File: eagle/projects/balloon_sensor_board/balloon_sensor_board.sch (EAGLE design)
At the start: 13 parts, among them J201 MOL-SL-4-RA, U1 PCT2075GVJ, U202 MS560702BA03-50

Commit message: cleaned up HAT and balloon_sensor for panelling
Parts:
- added TP202: (no value), daqcs:TEST_POINT_SMT_15R_SMD
- renumbered LOGO1 to LOGO201, LOGO2 to LOGO202, U1 to U201
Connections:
- net GND: now also TP201.TP
- net TEMP0_OS: now also TP202.TP; no longer TP201.TP
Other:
- note added: "1"
- note added: "DESIGN: 001-004-01"
- note removed: "A"
- moved on the sheet: TP201
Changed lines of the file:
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@@
 </variantdefs>
 <classes>
-<class number="0" name="default" width="0" drill="0">
+<class number="0" name="default" width="0" drill="0.381">
+<clearance class="0" value="0.1524"/>
 </class>
 </classes>
@@
 <part name="PP3V3201" library="daqcs" deviceset="PP3V3" device=""/>
 <part name="C201" library="daqcs" deviceset="CAP" device="_0603" technology="_1UF0" value="1uF"/>
-<part name="GND202" library="daqcs" deviceset="GND" device=""/>
+<part name="GND203" library="daqcs" deviceset="GND" device=""/>
 <part name="U202" library="daqcs" deviceset="MS5607" device="_8SMD" technology="-02BA03" value="MS560702BA03-50"/>
 <part name="R204" library="daqcs" deviceset="RES" device="_0603" technology="_0R0" value="0.0"/>
 <part name="C203" library="daqcs" deviceset="CAP" device="_0603" technology="_100NF0" value="100nF"/>
-<part name="GND204" library="daqcs" deviceset="GND" device=""/>
-<part name="GND206" library="daqcs" deviceset="GND" device=""/>
+<part name="GND205" library="daqcs" deviceset="GND" device=""/>
+<part name="GND207" library="daqcs" deviceset="GND" device=""/>
 <part name="GND209" library="daqcs" deviceset="GND" device=""/>
 <part name="C202" library="daqcs" deviceset="CAP" device="_0603" technology="_100NF0" value="100nF"/>
 <part name="R203" library="daqcs" deviceset="RES" device="_0603" technology="_0R0" value="0.0"/>
-<part name="GND205" library="daqcs" deviceset="GND" device=""/>
+<part name="GND206" library="daqcs" deviceset="GND" device=""/>
 <part name="GND208" library="daqcs" deviceset="GND" device=""/>
-<part name="GND203" library="daqcs" deviceset="GND" device=""/>
-<part name="TP201" library="daqcs" deviceset="TEST_POINT_SMT" device="_15R_SMD"/>
+<part name="GND204" library="daqcs" deviceset="GND" device=""/>
+<part name="TP202" library="daqcs" deviceset="TEST_POINT_SMT" device="_15R_SMD"/>
 <part name="PP3V3202" library="daqcs" deviceset="PP3V3" device=""/>
 <part name="PP3V3203" library="daqcs" deviceset="PP3V3" device=""/>
-<part name="U1" library="daqcs" deviceset="PCT2075GV" device="_TSOP6" value="PCT2075GVJ"/>
-<part name="LOGO1" library="daqcs" deviceset="SQUAD_LOGO" device=""/>
-<part name="LOGO2" library="daqcs" deviceset="CMS_LOGO" device=""/>
+<part name="U201" library="daqcs" deviceset="PCT2075GV" device="_TSOP6" value="PCT2075GVJ"/>
+<part name="LOGO201" library="daqcs" deviceset="SQUAD_LOGO" device=""/>
+<part name="LOGO202" library="daqcs" deviceset="CMS_LOGO" device=""/>
+<part name="TP201" library="daqcs" deviceset="TEST_POINT_SMT" device="_15R_SMD"/>
+<part name="GND202" library="daqcs" deviceset="GND" device=""/>
 </parts>
 <sheets>
@@
 <text x="81.28" y="182.88" size="3.81" layer="91">I2C_SENSORS</text>
 <text x="330.2" y="27.94" size="3.81" layer="91">TITLE_TOC</text>
-<text x="421.64" y="7.62" size="3.81" layer="91">A</text>
+<text x="421.64" y="7.62" size="3.81" layer="91">1</text>
 <text x="327.66" y="60.96" size="3.81" layer="91">ENGINEER: CHRIS SCHWAB</text>
 <text x="340.36" y="68.58" size="3.81" layer="91">TEAM: P17105</text>
+<text x="335.28" y="76.2" size="3.81" layer="91">DESIGN: 001-004-01</text>
 </plain>
 <instances>
@@
 <text x="86.36" y="251.46" size="11.43" layer="91">TEMP AND PRESSURE SENSORS</text>
 <text x="330.2" y="27.94" size="3.81" layer="91">I2C_SENSORS</text>
-<text x="421.64" y="7.62" size="3.81" layer="91">A</text>
+<text x="421.64" y="7.62" size="3.81" layer="91">1</text>
 <text x="243.84" y="109.22" size="3.81" layer="91">Pressure Sensor 0</text>
 <text x="231.14" y="50.8" size="1.778" layer="91">Complement of CSB</text>
@@
 <attribute name="VOLTAGE" x="75.819" y="161.544" size="1.778" layer="95" ratio="10" rot="R90"/>
 </instance>
-<instance part="GND202" gate="1" x="81.28" y="154.94"/>
+<instance part="GND203" gate="1" x="81.28" y="154.94"/>
 <instance part="U202" gate="G$1" x="251.46" y="78.74"/>
 <instance part="R204" gate="G$1" x="218.44" y="53.34" rot="R90"/>
@@
 <attribute name="VOLTAGE" x="225.679" y="87.884" size="1.778" layer="95" ratio="10" rot="R90"/>
 </instance>
-<instance part="GND204" gate="1" x="203.2" y="81.28"/>
-<instance part="GND206" gate="1" x="218.44" y="40.64"/>
+<instance part="GND205" gate="1" x="203.2" y="81.28"/>
+<instance part="GND207" gate="1" x="218.44" y="40.64"/>
 <instance part="GND209" gate="1" x="274.32" y="40.64"/>
 <instance part="C202" gate="G$1" x="215.9" y="190.5" smashed="yes" rot="R90">
@@
 </instance>
 <instance part="R203" gate="G$1" x="210.82" y="165.1" rot="R90"/>
-<instance part="GND205" gate="1" x="210.82" y="152.4"/>
+<instance part="GND206" gate="1" x="210.82" y="152.4"/>
 <instance part="GND208" gate="1" x="271.78" y="152.4"/>
-<instance part="GND203" gate="1" x="198.12" y="185.42"/>
-<instance part="TP201" gate="G$1" x="304.8" y="177.8" smashed="yes" rot="R270">
-<attribute name="NAME" x="309.88" y="179.07" size="1.778" layer="95" align="center"/>
+<instance part="GND204" gate="1" x="198.12" y="185.42"/>
+<instance part="TP202" gate="G$1" x="304.8" y="177.8" smashed="yes" rot="R270">
+<attribute name="NAME" x="312.42" y="179.07" size="1.778" layer="95" align="center"/>
 <attribute name="TP_SIGNAL_NAME" x="303.53" y="173.99" size="1.778" layer="97" rot="R270"/>
 </instance>
 <instance part="PP3V3202" gate="G$1" x="226.06" y="210.82"/>
 <instance part="PP3V3203" gate="G$1" x="228.6" y="106.68"/>
-<instance part="U1" gate="G$1" x="248.92" y="182.88"/>
-<instance part="LOGO1" gate="G$1" x="96.52" y="66.04"/>
-<instance part="LOGO2" gate="G$1" x="96.52" y="48.26"/>
+<instance part="U201" gate="G$1" x="248.92" y="182.88"/>
+<instance part="LOGO201" gate="G$1" x="96.52" y="66.04"/>
+<instance part="LOGO202" gate="G$1" x="96.52" y="48.26"/>
+<instance part="TP201" gate="G$1" x="81.28" y="119.38" smashed="yes" rot="R270">
+<attribute name="NAME" x="88.9" y="120.65" size="1.778" layer="95" align="center"/>
+<attribute name="TP_SIGNAL_NAME" x="80.01" y="115.57" size="1.778" layer="97" rot="R270"/>
+</instance>
+<instance part="GND202" gate="1" x="68.58" y="114.3"/>
 </instances>
 <busses>
@@
 <junction x="226.06" y="190.5"/>
 <pinref part="PP3V3202" gate="G$1" pin="PP3V3"/>
-<pinref part="U1" gate="G$1" pin="VCC"/>
+<pinref part="U201" gate="G$1" pin="VCC"/>
 </segment>
 <segment>
@@
 <segment>
 <pinref part="C201" gate="G$1" pin="2"/>
-<pinref part="GND202" gate="1" pin="GND"/>
+<pinref part="GND203" gate="1" pin="GND"/>
 <wire x1="71.12" y1="160.02" x2="81.28" y2="160.02" width="0.1524" layer="91"/>
 <wire x1="81.28" y1="160.02" x2="81.28" y2="157.48" width="0.1524" layer="91"/>
 </segment>
 <segment>
-<pinref part="GND204" gate="1" pin="GND"/>
+<pinref part="GND205" gate="1" pin="GND"/>
 <pinref part="C203" gate="G$1" pin="1"/>
 <wire x1="203.2" y1="83.82" x2="203.2" y2="86.36" width="0.1524" layer="91"/>
@@
 <segment>
 <pinref part="R204" gate="G$1" pin="1"/>
-<pinref part="GND206" gate="1" pin="GND"/>
+<pinref part="GND207" gate="1" pin="GND"/>
 <wire x1="218.44" y1="48.26" x2="218.44" y2="43.18" width="0.1524" layer="91"/>
 </segment>
@@
 <pinref part="C202" gate="G$1" pin="1"/>
 <wire x1="210.82" y1="190.5" x2="198.12" y2="190.5" width="0.1524" layer="91"/>
-<pinref part="GND203" gate="1" pin="GND"/>
+<pinref part="GND204" gate="1" pin="GND"/>
 <wire x1="198.12" y1="190.5" x2="198.12" y2="187.96" width="0.1524" layer="91"/>
 </segment>
 <segment>
-<pinref part="GND205" gate="1" pin="GND"/>
+<pinref part="GND206" gate="1" pin="GND"/>
 <pinref part="R203" gate="G$1" pin="1"/>
 <wire x1="210.82" y1="154.94" x2="210.82" y2="160.02" width="0.1524" layer="91"/>
@@
 <pinref part="GND208" gate="1" pin="GND"/>
 <wire x1="271.78" y1="170.18" x2="271.78" y2="154.94" width="0.1524" layer="91"/>
-<pinref part="U1" gate="G$1" pin="GND"/>
+<pinref part="U201" gate="G$1" pin="GND"/>
+</segment>
+<segment>
+<pinref part="GND202" gate="1" pin="GND"/>
+<pinref part="TP201" gate="G$1" pin="TP"/>
+<wire x1="68.58" y1="116.84" x2="68.58" y2="119.38" width="0.1524" layer="91"/>
+<wire x1="68.58" y1="119.38" x2="76.2" y2="119.38" width="0.1524" layer="91"/>
 </segment>
 </net>
@@
 <wire x1="266.7" y1="185.42" x2="299.72" y2="185.42" width="0.1524" layer="91"/>
 <label x="271.78" y="185.42" size="1.778" layer="95"/>
-<pinref part="U1" gate="G$1" pin="SCL"/>
+<pinref part="U201" gate="G$1" pin="SCL"/>
 </segment>
 </net>
@@
 <wire x1="266.7" y1="190.5" x2="299.72" y2="190.5" width="0.1524" layer="91"/>
 <label x="271.78" y="190.5" size="1.778" layer="95"/>
-<pinref part="U1" gate="G$1" pin="SDA"/>
+<pinref part="U201" gate="G$1" pin="SDA"/>
 </segment>
 </net>
@@
 <wire x1="210.82" y1="180.34" x2="231.14" y2="180.34" width="0.1524" layer="91"/>
 <label x="210.82" y="180.34" size="1.778" layer="95"/>
-<pinref part="U1" gate="G$1" pin="A0"/>
+<pinref part="U201" gate="G$1" pin="A0"/>
 </segment>
 </net>
 <net name="TEMP0_OS" class="0">
 <segment>
-<pinref part="TP201" gate="G$1" pin="TP"/>
+<pinref part="TP202" gate="G$1" pin="TP"/>
 <wire x1="266.7" y1="177.8" x2="299.72" y2="177.8" width="0.1524" layer="91"/>
 <label x="271.78" y="177.8" size="1.778" layer="95"/>
-<pinref part="U1" gate="G$1" pin="OS"/>
-</segment>
-</net>
+<pinref part="U201" gate="G$1" pin="OS"/>
+</segment>
+</net>

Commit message: added panels
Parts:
- added R205, R206: 0.0, daqcs:RES_0R0_0603
- added TP203: (no value), daqcs:TEST_POINT_SMT_15R_SMD
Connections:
- removed net TEMP0_I2C_A0: R203.2, U201.A0
- new net TEMP0_A0: R205.1, R206.2, U201.A0
- net GND: now also R206.1, TP202.TP; no longer R203.1, TP201.TP
- net PP3V3: now also R203.2, R205.2, TP201.TP
- net PRES0_CSB: now also R203.1
- net TEMP0_OS: now also TP203.TP; no longer TP202.TP
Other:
- moved on the sheet: C203, R203, R204, TP201, TP202

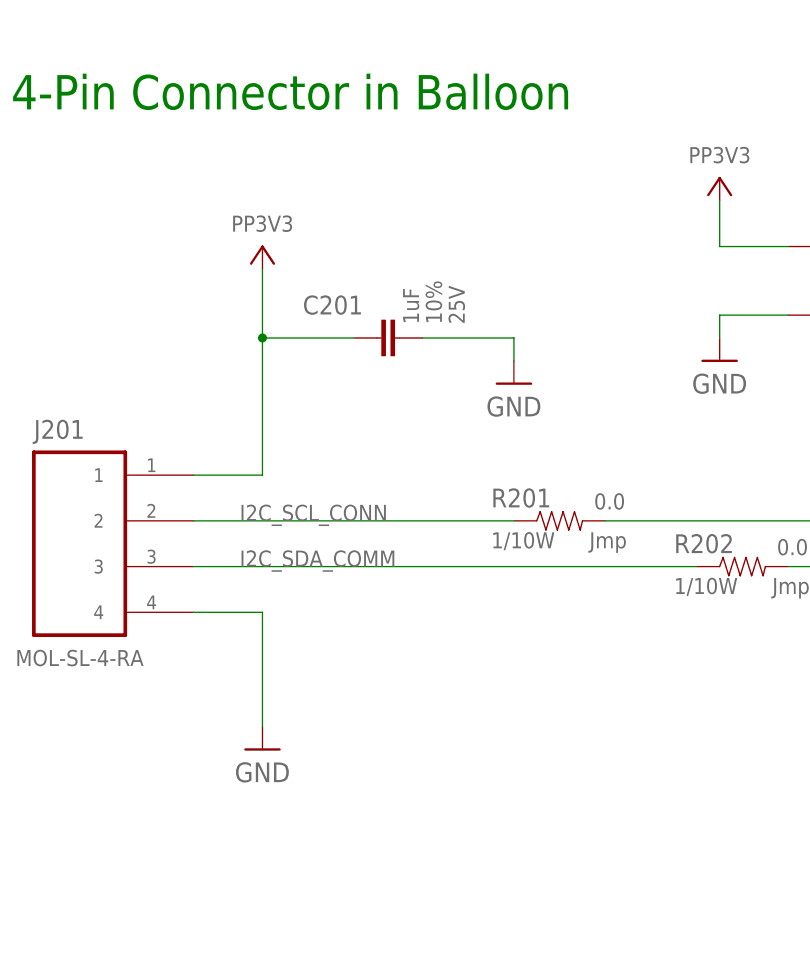
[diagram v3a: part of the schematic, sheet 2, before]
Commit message: adding all finalized gerber, schem, and bom files for Rev1 of HAT and balloon sensor boards
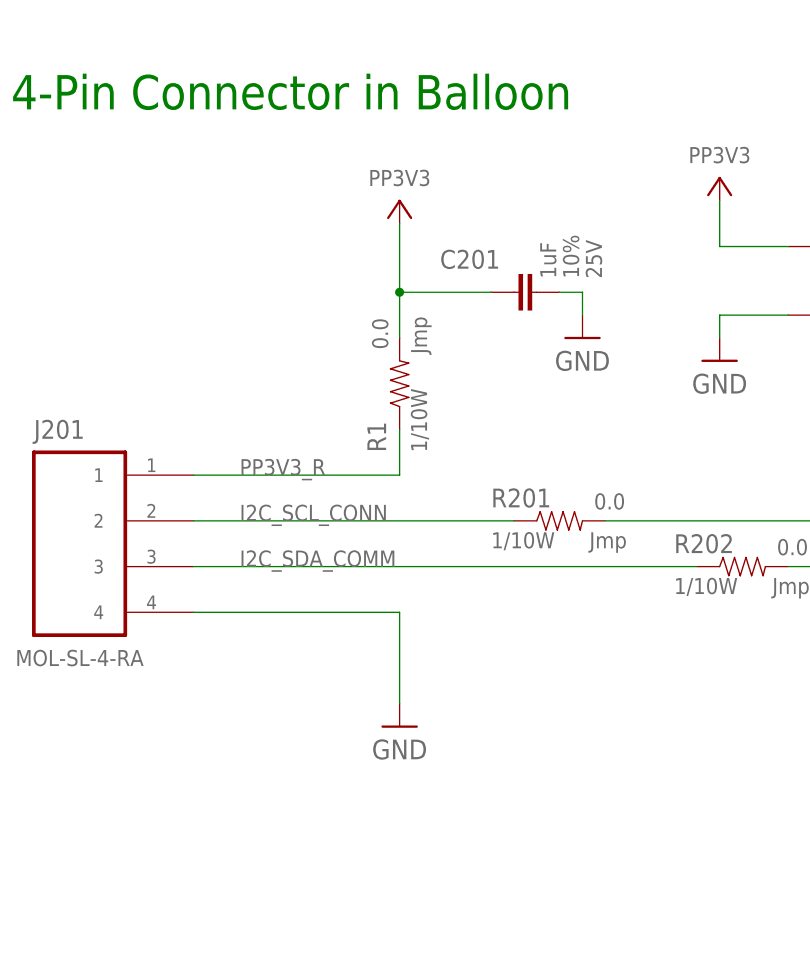
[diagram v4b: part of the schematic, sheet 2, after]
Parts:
- added R1: 0.0, daqcs:RES_0R0_0603
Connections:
- new net PP3V3_R: J201.1, R1.1
- net PP3V3: now also R1.2; no longer J201.1
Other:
- moved on the sheet: C201
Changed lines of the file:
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@@
 </attributes>
 <variantdefs>
+<variantdef name="POR" current="yes"/>
 </variantdefs>
 <classes>
@@
 <part name="TP201" library="daqcs" deviceset="TEST_POINT_SMT" device="_15R_SMD"/>
 <part name="PP3V3202" library="daqcs" deviceset="PP3V3" device=""/>
-<part name="R205" library="daqcs" deviceset="RES" device="_0603" technology="_0R0" value="0.0"/>
-<part name="R203" library="daqcs" deviceset="RES" device="_0603" technology="_0R0" value="0.0"/>
+<part name="R205" library="daqcs" deviceset="RES" device="_0603" technology="_0R0" value="0.0">
+<variant name="POR" populate="no"/>
+</part>
+<part name="R203" library="daqcs" deviceset="RES" device="_0603" technology="_0R0" value="0.0">
+<variant name="POR" populate="no"/>
+</part>
+<part name="R1" library="daqcs" deviceset="RES" device="_0603" technology="_0R0" value="0.0"/>
 </parts>
 <sheets>
@@
 <instance part="R201" gate="G$1" x="86.36" y="139.7"/>
 <instance part="R202" gate="G$1" x="106.68" y="134.62"/>
-<instance part="GND201" gate="1" x="53.34" y="114.3"/>
-<instance part="PP3V3201" gate="G$1" x="53.34" y="170.18"/>
-<instance part="C201" gate="G$1" x="68.58" y="160.02" smashed="yes" rot="R90">
-<attribute name="NAME" x="64.516" y="164.719" size="2.0828" layer="95" ratio="10" rot="R180"/>
-<attribute name="VALUE" x="70.739" y="161.544" size="1.778" layer="96" ratio="10" rot="R90"/>
-<attribute name="TOLERANCE" x="73.279" y="161.544" size="1.778" layer="95" ratio="10" rot="R90"/>
-<attribute name="VOLTAGE" x="75.819" y="161.544" size="1.778" layer="95" ratio="10" rot="R90"/>
-</instance>
-<instance part="GND202" gate="1" x="81.28" y="154.94"/>
+<instance part="GND201" gate="1" x="68.58" y="116.84"/>
+<instance part="PP3V3201" gate="G$1" x="68.58" y="175.26"/>
+<instance part="C201" gate="G$1" x="83.82" y="165.1" smashed="yes" rot="R90">
+<attribute name="NAME" x="79.756" y="169.799" size="2.0828" layer="95" ratio="10" rot="R180"/>
+<attribute name="VALUE" x="85.979" y="166.624" size="1.778" layer="96" ratio="10" rot="R90"/>
+<attribute name="TOLERANCE" x="88.519" y="166.624" size="1.778" layer="95" ratio="10" rot="R90"/>
+<attribute name="VOLTAGE" x="91.059" y="166.624" size="1.778" layer="95" ratio="10" rot="R90"/>
+</instance>
+<instance part="GND202" gate="1" x="88.9" y="160.02"/>
 <instance part="U202" gate="G$1" x="251.46" y="78.74"/>
 <instance part="R204" gate="G$1" x="215.9" y="53.34" rot="R90"/>
@@
 <instance part="R205" gate="G$1" x="223.52" y="180.34" rot="R90"/>
 <instance part="R203" gate="G$1" x="215.9" y="83.82" rot="R90"/>
+<instance part="R1" gate="G$1" x="68.58" y="154.94" rot="R90"/>
 </instances>
 <busses>
@@
 <net name="PP3V3" class="0">
 <segment>
-<pinref part="J201" gate="G$1" pin="1"/>
 <pinref part="PP3V3201" gate="G$1" pin="PP3V3"/>
-<wire x1="45.72" y1="144.78" x2="53.34" y2="144.78" width="0.1524" layer="91"/>
-<wire x1="53.34" y1="144.78" x2="53.34" y2="160.02" width="0.1524" layer="91"/>
 <pinref part="C201" gate="G$1" pin="1"/>
-<wire x1="53.34" y1="160.02" x2="53.34" y2="167.64" width="0.1524" layer="91"/>
-<wire x1="63.5" y1="160.02" x2="53.34" y2="160.02" width="0.1524" layer="91"/>
-<junction x="53.34" y="160.02"/>
+<wire x1="68.58" y1="165.1" x2="68.58" y2="172.72" width="0.1524" layer="91"/>
+<wire x1="78.74" y1="165.1" x2="68.58" y2="165.1" width="0.1524" layer="91"/>
+<pinref part="R1" gate="G$1" pin="2"/>
+<wire x1="68.58" y1="160.02" x2="68.58" y2="165.1" width="0.1524" layer="91"/>
+<junction x="68.58" y="165.1"/>
 </segment>
 <segment>
@@
 <pinref part="J201" gate="G$1" pin="4"/>
 <pinref part="GND201" gate="1" pin="GND"/>
-<wire x1="45.72" y1="129.54" x2="53.34" y2="129.54" width="0.1524" layer="91"/>
-<wire x1="53.34" y1="129.54" x2="53.34" y2="116.84" width="0.1524" layer="91"/>
+<wire x1="45.72" y1="129.54" x2="68.58" y2="129.54" width="0.1524" layer="91"/>
+<wire x1="68.58" y1="129.54" x2="68.58" y2="119.38" width="0.1524" layer="91"/>
 </segment>
 <segment>
 <pinref part="C201" gate="G$1" pin="2"/>
 <pinref part="GND202" gate="1" pin="GND"/>
-<wire x1="71.12" y1="160.02" x2="81.28" y2="160.02" width="0.1524" layer="91"/>
-<wire x1="81.28" y1="160.02" x2="81.28" y2="157.48" width="0.1524" layer="91"/>
+<wire x1="86.36" y1="165.1" x2="88.9" y2="165.1" width="0.1524" layer="91"/>
+<wire x1="88.9" y1="165.1" x2="88.9" y2="162.56" width="0.1524" layer="91"/>
 </segment>
 <segment>
@@
 </segment>
 </net>
+<net name="PP3V3_R" class="0">
+<segment>
+<pinref part="J201" gate="G$1" pin="1"/>
+<wire x1="45.72" y1="144.78" x2="68.58" y2="144.78" width="0.1524" layer="91"/>
+<pinref part="R1" gate="G$1" pin="1"/>
+<wire x1="68.58" y1="149.86" x2="68.58" y2="144.78" width="0.1524" layer="91"/>
+<label x="50.8" y="144.78" size="1.778" layer="95"/>
+</segment>
+</net>

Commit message: added modified BOMs to remove non-component parts, samples, and column for a board instance multiplier
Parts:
- added BOM1: SL 70066 4PIN HOUSING, daqcs:BOM_LINE_ITEM_BLI4
- added BOM2, BOM3, BOM4, BOM5: SL 70058 GOLD CRIMP, daqcs:BOM_LINE_ITEM_BLI6
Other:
- note added: "ASSEMBLY_COMPONENTS"
- note added: "Connector Assembly"
- note added: "J201 4-pin SL Connector:"
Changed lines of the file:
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@@
 </attributes>
 <variantdefs>
-<variantdef name="POR" current="yes"/>
+<variantdef name="POR"/>
 </variantdefs>
 <classes>
@@
 </part>
 <part name="R1" library="daqcs" deviceset="RES" device="_0603" technology="_0R0" value="0.0"/>
+<part name="FRAME1" library="daqcs" deviceset="FRAME_B_L" device=""/>
+<part name="BOM1" library="daqcs" deviceset="BOM_LINE_ITEM" device="" technology="_BLI4" value="SL 70066 4PIN HOUSING"/>
+<part name="BOM2" library="daqcs" deviceset="BOM_LINE_ITEM" device="" technology="_BLI6" value="SL 70058 GOLD CRIMP"/>
+<part name="BOM3" library="daqcs" deviceset="BOM_LINE_ITEM" device="" technology="_BLI6" value="SL 70058 GOLD CRIMP"/>
+<part name="BOM4" library="daqcs" deviceset="BOM_LINE_ITEM" device="" technology="_BLI6" value="SL 70058 GOLD CRIMP"/>
+<part name="BOM5" library="daqcs" deviceset="BOM_LINE_ITEM" device="" technology="_BLI6" value="SL 70058 GOLD CRIMP"/>
 </parts>
 <sheets>
@@
 <text x="340.36" y="68.58" size="3.81" layer="91">TEAM: P17105</text>
 <text x="335.28" y="76.2" size="3.81" layer="91">DESIGN: 001-004-01</text>
+<text x="81.28" y="175.26" size="3.81" layer="91">ASSEMBLY_COMPONENTS</text>
 </plain>
 <instances>
@@
 </nets>
 </sheet>
+<sheet>
+<description>ASSEMBLY_COMPONENTS</description>
+<plain>
+<text x="330.2" y="27.94" size="3.81" layer="91">ASSEMBLY_COMPONENTS</text>
+<text x="421.64" y="7.62" size="3.81" layer="91">1</text>
+<text x="127" y="251.46" size="11.43" layer="91">Connector Assembly</text>
+<text x="182.88" y="228.6" size="3.81" layer="91">J201 4-pin SL Connector:</text>
+</plain>
+<instances>
+<instance part="FRAME1" gate="G$1" x="0" y="0"/>
+<instance part="FRAME1" gate="G$2" x="325.12" y="0"/>
+<instance part="BOM1" gate="G$1" x="167.64" y="213.36"/>
+<instance part="BOM2" gate="G$1" x="167.64" y="210.82"/>
+<instance part="BOM3" gate="G$1" x="167.64" y="208.28"/>
+<instance part="BOM4" gate="G$1" x="167.64" y="205.74"/>
+<instance part="BOM5" gate="G$1" x="167.64" y="203.2"/>
+</instances>
+<busses>
+</busses>
+<nets>
+</nets>
+</sheet>
